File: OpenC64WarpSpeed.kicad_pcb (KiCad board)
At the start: 2 copper layers, 58.4 x 61.7 mm, 17 parts, among them P1 C64-Exp-Port, SW1 SW_C64_C128, SW2 SW_Push, U1 74LS109, U2 27128

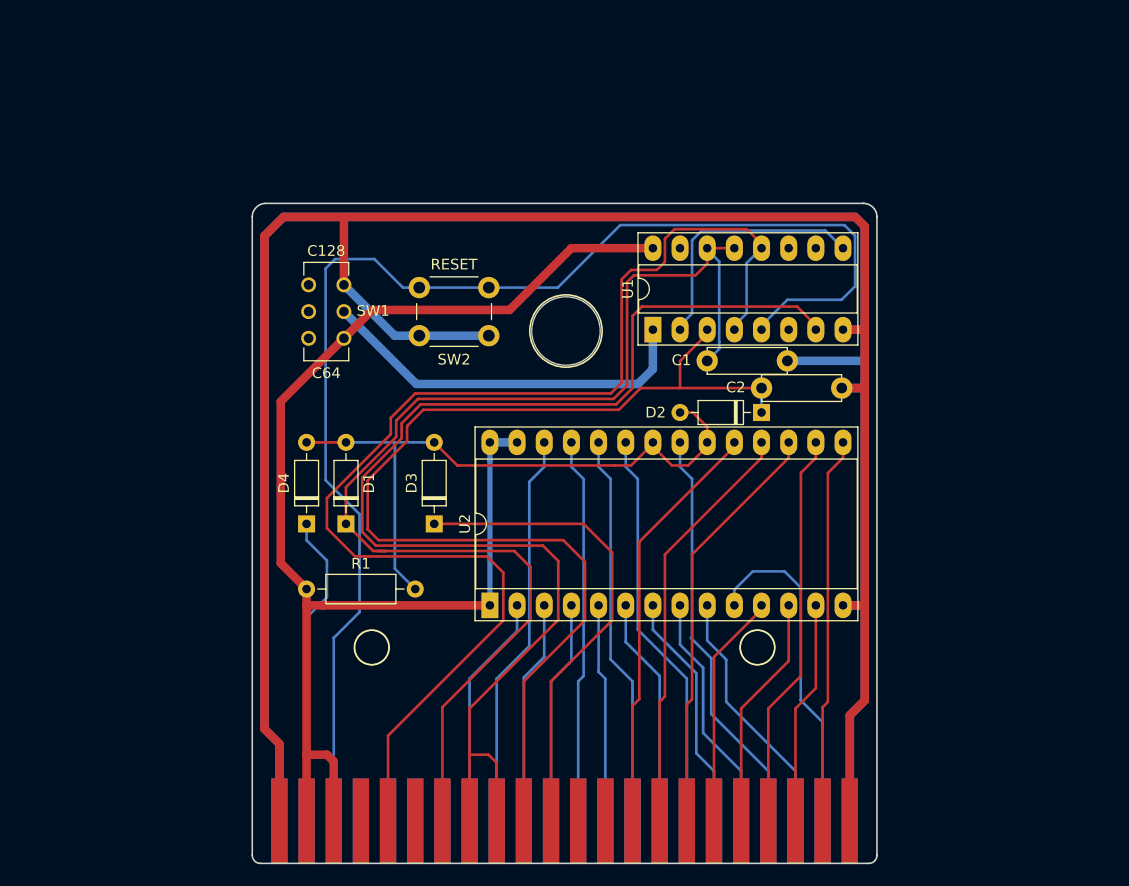
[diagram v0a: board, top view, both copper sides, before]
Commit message: Improving the design... - Use ground plane - Add decoupling caps - Avoid scrambling the address and data buses - Switch to 27512
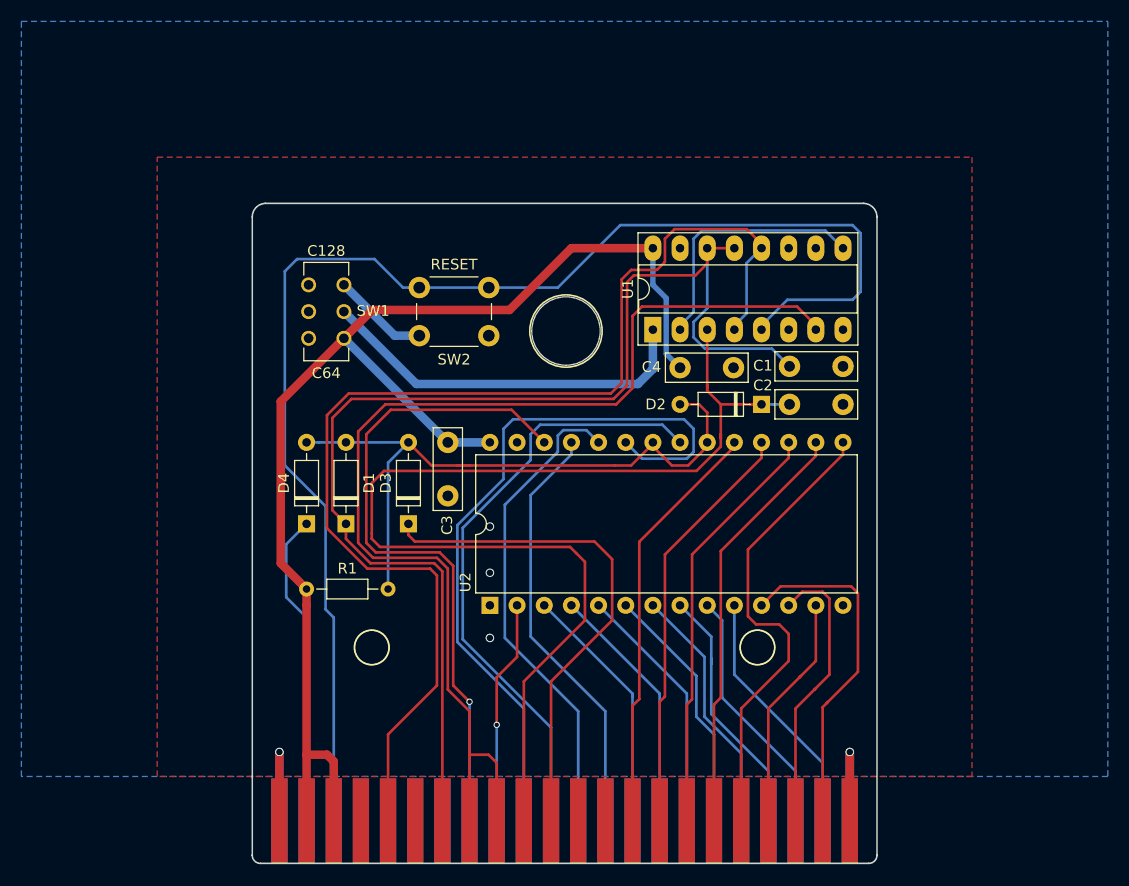
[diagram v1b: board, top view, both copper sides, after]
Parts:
- removed G***: LOGO, OpenC64WarpSpeed:Bottom
- removed G***: LOGO, OpenC64WarpSpeed:Top
- added C3: 100n, Capacitor_THT:C_Disc_D7.5mm_W2.5mm_P5.00mm, F.Cu at (78.0, 90.2)
- added C4: 100n, Capacitor_THT:C_Disc_D7.5mm_W2.5mm_P5.00mm, F.Cu at (99.7, 83.2)
- C1, C2: footprint OpenC64WarpSpeed:C_Disc_D7.5mm_W2.50mm_P7.50mm -> Capacitor_THT:C_Disc_D7.5mm_W2.5mm_P5.00mm
- R1: footprint Resistor_THT:R_Axial_DIN0207_L6.3mm_D2.5mm_P10.16mm_Horizontal -> Resistor_THT:R_Axial_DIN0204_L3.6mm_D1.6mm_P7.62mm_Horizontal
- U2: value 27128 -> 27512; footprint Package_DIP:DIP-28_W15.24mm_Socket_LongPads -> Package_DIP:DIP-28_W15.24mm
- moved C1 7.72 mm to (109.9, 83.1)
- moved C2 3.03 mm to (109.9, 86.6)
- moved D3 2.41 mm to (74.3, 97.8)
- moved D2 0.76 mm to (107.3, 86.6)
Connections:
- U2 pad 1: +5V -> GND
- U2 pad 11: /d4 -> /d0
- U2 pad 12: /d3 -> /d1
- U2 pad 13: /d1 -> /d2
- U2 pad 15: /d0 -> /d3
- U2 pad 16: /d2 -> /d4
- U2 pad 2: /a13 -> /a12
- U2 pad 21: /a2 -> /a10
- U2 pad 23: /a5 -> /a11
- U2 pad 24: /a7 -> /a9
- U2 pad 25: /a9 -> /a8
- U2 pad 26: /a12 -> /a13
- U2 pad 27: +5V -> (no net)
- U2 pad 3: /a11 -> /a7
- U2 pad 4: /a10 -> /a6
- U2 pad 5: /a8 -> /a5
- U2 pad 6: /a6 -> /a4
- U2 pad 7: /a4 -> /a3
- U2 pad 8: /a3 -> /a2
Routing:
- net GND: track 377.9 -> 34.8 mm, vias 0 -> 5
- net /a11: track 21.0 -> 69.0 mm
- net /a13: track 22.0 -> 62.5 mm, vias 0 -> 1
- net /a10: track 21.0 -> 57.3 mm
- net /d3: track 22.0 -> 43.8 mm
- net /a8: track 20.5 -> 39.9 mm
- net /d4: track 22.0 -> 39.4 mm
- net /a12: track 37.3 -> 21.0 mm, vias 0 -> 1
- net /d2: track 37.3 -> 22.2 mm
- net /a2: track 38.9 -> 24.1 mm
- net /a5: track 37.8 -> 23.6 mm
- net /a7: track 36.7 -> 23.6 mm
- net Net-(P1-Pad8): track 115.6 -> 105.3 mm
- net /a9: track 36.1 -> 45.5 mm
- net /a0: track 31.7 -> 23.6 mm
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- added copper zone on B.Cu, net GND
- added copper zone on F.Cu, net GND

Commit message: Almost there
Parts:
- U2: footprint Package_DIP:DIP-28_W15.24mm -> Package_DIP:DIP-28_W15.24mm_Socket_LongPads
- moved D2 37.9 mm to (71.1, 97.8), turned to 90 degrees
- moved C3 1.29 mm to (98.4, 83.2)
- moved D1 0.51 mm to (67.9, 97.8)
- renumbered C4 to C3, C3 to C4
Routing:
- net Net-(C2-Pad1): track 106.3 -> 116.8 mm
- net Net-(D1-Pad2): track 62.9 -> 57.2 mm
- net Net-(P1-Pad5): track 112.0 -> 114.1 mm
- net Net-(SW1-Pad2): track 36.0 -> 34.0 mm
- net Net-(C1-Pad1): track 115.1 -> 116.9 mm
- net Net-(P1-Pad8): track 105.3 -> 106.2 mm
- net /a13: track 62.5 -> 63.2 mm
- net /a2: track 24.1 -> 23.6 mm

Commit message: I guess we're good, just need to work on the ground plane yet
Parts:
- added SW3: SW_ROM, OpenC64WarpSpeed:SW_DPDT, F.Cu at (70.7, 79.9)
- SW2: value SW_Push -> SW_RESET
- moved SW2 1.99 mm to (77.2, 75.1)
- moved SW1 0.59 mm to (68.1, 74.9)
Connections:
- U2 pad 27: (no net) -> Net-(SW3-Pad2)
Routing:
- net Net-(SW3-Pad2): track 0.00 -> 22.3 mm, vias 0 -> 1
- net +5V: track 119.1 -> 136.2 mm
- net GND: track 34.8 -> 25.8 mm
- net Net-(SW1-Pad2): track 34.0 -> 39.9 mm
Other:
- board text added: "ROM1"
- board text added: "ROM2"

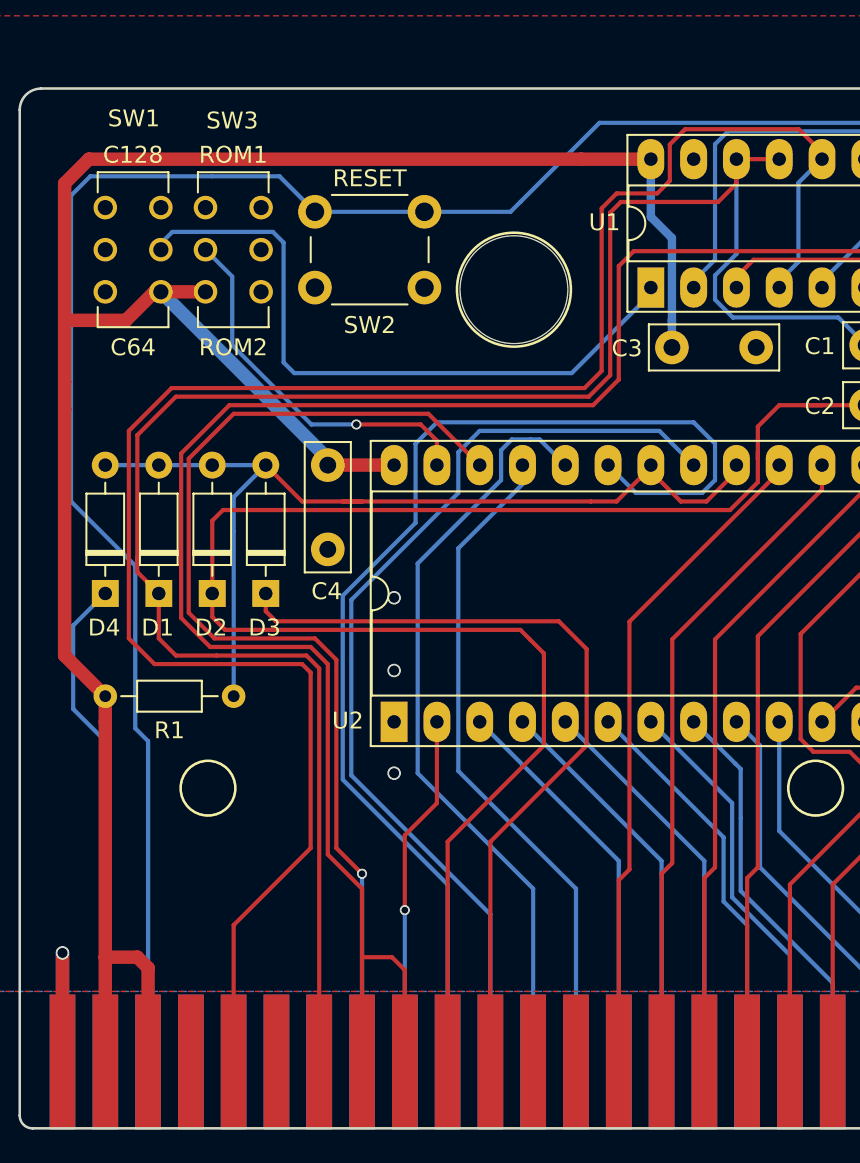
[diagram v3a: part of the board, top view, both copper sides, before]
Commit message: Switch to a 27256 EPROM, but a 27512 can still be used (use upper 32K)
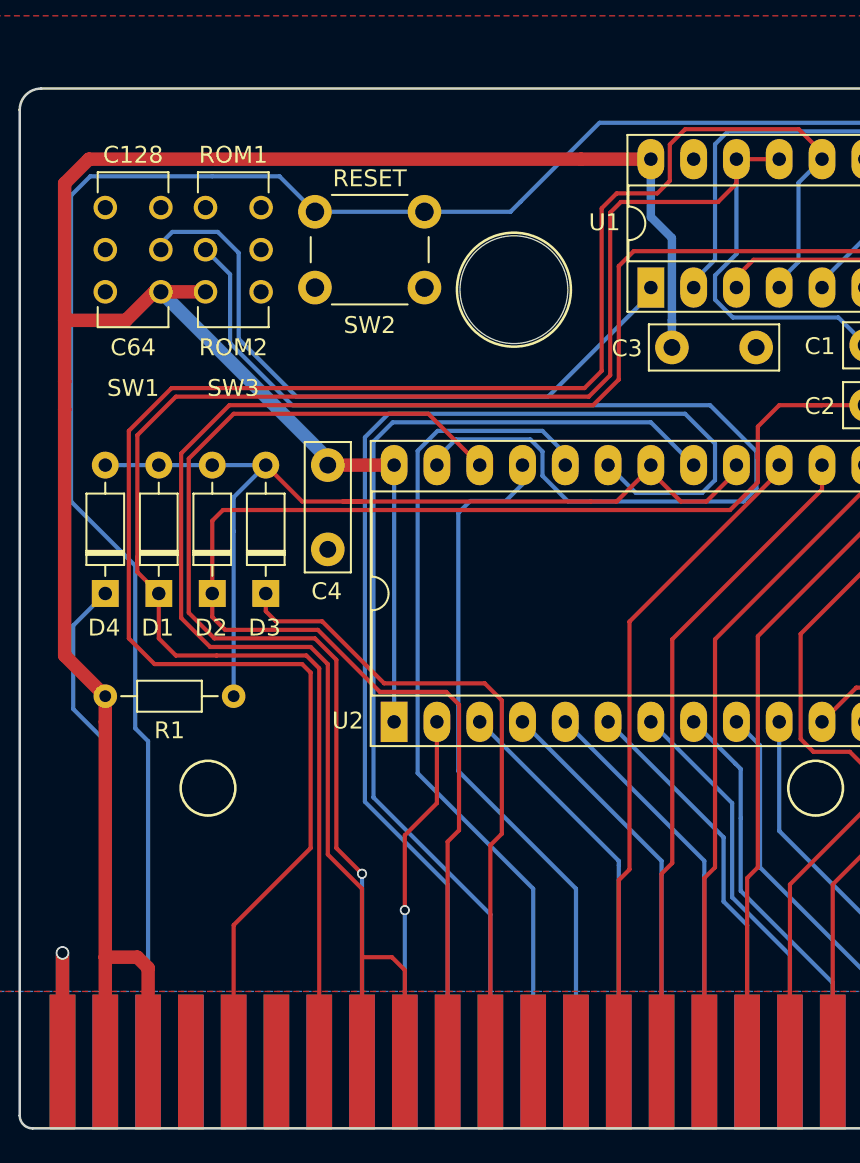
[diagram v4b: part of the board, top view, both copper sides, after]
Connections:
- U2 pad 1: GND -> +5V
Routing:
- net Net-(SW3-Pad2): track 22.3 -> 64.8 mm, vias 1 -> 0
- net +5V: track 136.2 -> 151.4 mm
- net Net-(C2-Pad1): track 116.8 -> 107.9 mm
- net /~roml: track 47.9 -> 39.0 mm
- net /a9: track 45.9 -> 49.6 mm
- net /a10: track 57.6 -> 60.2 mm
- net /a11: track 69.4 -> 70.7 mm
- net /a8: track 39.9 -> 41.1 mm
- net GND: vias 5 -> 2

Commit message: Yeah
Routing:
- net +5V: track 151.4 -> 145.6 mm
- net Net-(D1-Pad2): track 57.2 -> 59.6 mm
- net GND: vias 2 -> 39
